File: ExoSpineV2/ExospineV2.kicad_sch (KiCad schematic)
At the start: 49 parts, among them J1 GPIO, J15 Conn_01x02, J16 Conn_01x02, J17 Conn_01x02, J19 Conn_01x03, J20 Conn_01x03, J21 Conn_01x03, J22 Conn_01x02, J23 Conn_01x02, J24 Conn_01x02, J25 Conn_01x03, J26 JST PH 3pin, J27 Conn_01x04, J29 Conn_01x03, J30 Conn_01x02, J34 Conn_01x03, Q10 Q_NMOS_DGS, Q11 Q_NMOS_DGS, Q6 Q_NMOS_DGS, Q7 Q_NMOS_DGS, Q8 Q_NMOS_DGS, Q9 Q_NMOS_DGS, U4 74HC00, U5 74HC00, U6 MCP3008, U7 LTC2944, U8 LTC2944

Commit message: added connectors
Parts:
- J15, J16, J17, J22, J23, J24, J30: value Conn_01x02 -> JST PH 2pin; footprint (none) -> Connector_JST:JST_PH_B2B-PH-K_1x02_P2.00mm_Vertical
- J19, J20, J21, J25, J29, J34: value Conn_01x03 -> JST PH 3pin; footprint (none) -> Connector_JST:JST_PH_B3B-PH-K_1x03_P2.00mm_Vertical
- J26: footprint Connector_JST:JST_PH_B2B-PH-K_1x02_P2.00mm_Vertical -> Connector_JST:JST_PH_B3B-PH-K_1x03_P2.00mm_Vertical
- J27: value Conn_01x04 -> JST PH 4pin; footprint (none) -> Connector_JST:JST_PH_B4B-PH-K_1x04_P2.00mm_Vertical
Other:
- note added: "Batterie Feedback Switch - 0 for 12V Battery - 1 for 24V Battery"
- note removed: "12V Batterie I2C Enable"
- note removed: "24V Batterie I2C Enable"
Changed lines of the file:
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@@
     (fill (type none))
   )
-  (arc (start 46.936 71.123) (mid 46.1743 68.5836) (end 46.932 66.043)
+  (arc (start 46.99 68.58) (mid 46.4298 67.3236) (end 46.932 66.043)
     (stroke (width 0) (type default) (color 132 132 132 1))
     (fill (type none))
@@
     (effects (font (size 1.27 1.27)) (justify left bottom))
   )
-  (text "12V Batterie I2C Enable" (at 45.72 68.58 0)
-    (effects (font (size 1.27 1.27) (color 132 132 132 1)) (justify right bottom))
-  )
   (text "Button" (at 119.38 66.04 0)
     (effects (font (size 1.27 1.27) (color 132 132 132 1)) (justify left bottom))
@@
     (effects (font (size 1.27 1.27)) (justify left bottom))
   )
-  (text "24V Batterie I2C Enable" (at 45.72 71.12 0)
-    (effects (font (size 1.27 1.27) (color 132 132 132 1)) (justify right bottom))
-  )
   (text "Actuator Feedback 2" (at 299.72 177.8 0)
     (effects (font (size 1.27 1.27)) (justify left bottom))
@@
     (effects (font (size 1.27 1.27) (color 132 132 132 1)) (justify left bottom))
   )
+  (text "Batterie Feedback Switch\n- 0 for 12V Battery\n- 1 for 24V Battery"
+    (at 21.59 72.39 0)
+    (effects (font (size 1.27 1.27) (color 132 132 132 1)) (justify left bottom))
+  )
   (text "SN74HC00DR" (at 316.23 185.42 0)
     (effects (font (size 1.27 1.27) (color 0 194 0 1)) (justify left bottom))
@@
       (effects (font (size 1.27 1.27)) (justify left))
     )
-    (property "Value" "Conn_01x02" (at 346.71 33.02 0)
+    (property "Value" "JST PH 2pin" (at 346.71 33.02 0)
       (effects (font (size 1.27 1.27)) (justify left))
     )
-    (property "Footprint" "" (at 344.17 30.48 0)
+    (property "Footprint" "Connector_JST:JST_PH_B2B-PH-K_1x02_P2.00mm_Vertical" (at 344.17 30.48 0)
       (effects (font (size 1.27 1.27)) hide)
     )
@@
       (effects (font (size 1.27 1.27)) (justify left))
     )
-    (property "Value" "Conn_01x03" (at 284.48 191.77 0)
+    (property "Value" "JST PH 3pin" (at 284.48 191.77 0)
       (effects (font (size 1.27 1.27)) (justify left))
     )
-    (property "Footprint" "" (at 281.94 190.5 0)
+    (property "Footprint" "Connector_JST:JST_PH_B3B-PH-K_1x03_P2.00mm_Vertical" (at 281.94 190.5 0)
       (effects (font (size 1.27 1.27)) hide)
     )
@@
       (effects (font (size 1.27 1.27)) (justify left))
     )
-    (property "Value" "Conn_01x02" (at 250.19 69.85 0)
+    (property "Value" "JST PH 2pin" (at 250.19 69.85 0)
       (effects (font (size 1.27 1.27)) (justify left))
     )
-    (property "Footprint" "" (at 247.65 67.31 0)
+    (property "Footprint" "Connector_JST:JST_PH_B2B-PH-K_1x02_P2.00mm_Vertical" (at 247.65 67.31 0)
       (effects (font (size 1.27 1.27)) hide)
     )
@@
       (effects (font (size 1.27 1.27)) (justify left))
     )
-    (property "Value" "Conn_01x03" (at 304.8 156.21 0)
+    (property "Value" "JST PH 3pin" (at 304.8 156.21 0)
       (effects (font (size 1.27 1.27)) (justify left))
     )
-    (property "Footprint" "" (at 302.26 154.94 0)
+    (property "Footprint" "Connector_JST:JST_PH_B3B-PH-K_1x03_P2.00mm_Vertical" (at 302.26 154.94 0)
       (effects (font (size 1.27 1.27)) hide)
     )
@@
       (effects (font (size 1.27 1.27)) (justify left))
     )
-    (property "Value" "Conn_01x03" (at 374.65 191.77 0)
+    (property "Value" "JST PH 3pin" (at 374.65 191.77 0)
       (effects (font (size 1.27 1.27)) (justify left))
     )
-    (property "Footprint" "" (at 372.11 190.5 0)
+    (property "Footprint" "Connector_JST:JST_PH_B3B-PH-K_1x03_P2.00mm_Vertical" (at 372.11 190.5 0)
       (effects (font (size 1.27 1.27)) hide)
     )
@@
       (effects (font (size 1.27 1.27)) (justify left))
     )
-    (property "Footprint" "Connector_JST:JST_PH_B2B-PH-K_1x02_P2.00mm_Vertical" (at 284.48 33.02 0)
+    (property "Footprint" "Connector_JST:JST_PH_B3B-PH-K_1x03_P2.00mm_Vertical" (at 284.48 33.02 0)
       (effects (font (size 1.27 1.27)) hide)
     )
@@
       (effects (font (size 1.27 1.27)) (justify left))
     )
-    (property "Value" "Conn_01x03" (at 361.95 156.21 0)
+    (property "Value" "JST PH 3pin" (at 361.95 156.21 0)
       (effects (font (size 1.27 1.27)) (justify left))
     )
-    (property "Footprint" "" (at 359.41 154.94 0)
+    (property "Footprint" "Connector_JST:JST_PH_B3B-PH-K_1x03_P2.00mm_Vertical" (at 359.41 154.94 0)
       (effects (font (size 1.27 1.27)) hide)
     )
@@
       (effects (font (size 1.27 1.27)) (justify left))
     )
-    (property "Value" "Conn_01x03" (at 408.94 36.83 0)
+    (property "Value" "JST PH 3pin" (at 408.94 36.83 0)
       (effects (font (size 1.27 1.27)) (justify left))
     )
-    (property "Footprint" "" (at 406.4 35.56 0)
+    (property "Footprint" "Connector_JST:JST_PH_B3B-PH-K_1x03_P2.00mm_Vertical" (at 406.4 35.56 0)
       (effects (font (size 1.27 1.27)) hide)
     )
@@
       (effects (font (size 1.27 1.27)) (justify left))
     )
-    (property "Value" "Conn_01x02" (at 364.49 111.76 0)
+    (property "Value" "JST PH 2pin" (at 364.49 111.76 0)
       (effects (font (size 1.27 1.27)) (justify left))
     )
-    (property "Footprint" "" (at 361.95 109.22 0)
+    (property "Footprint" "Connector_JST:JST_PH_B2B-PH-K_1x02_P2.00mm_Vertical" (at 361.95 109.22 0)
       (effects (font (size 1.27 1.27)) hide)
     )
@@
       (effects (font (size 1.27 1.27)) (justify left))
     )
-    (property "Value" "Conn_01x02" (at 250.19 111.76 0)
+    (property "Value" "JST PH 2pin" (at 250.19 111.76 0)
       (effects (font (size 1.27 1.27)) (justify left))
     )
-    (property "Footprint" "" (at 247.65 109.22 0)
+    (property "Footprint" "Connector_JST:JST_PH_B2B-PH-K_1x02_P2.00mm_Vertical" (at 247.65 109.22 0)
       (effects (font (size 1.27 1.27)) hide)
     )
@@
       (effects (font (size 1.27 1.27)) (justify left))
     )
-    (property "Value" "Conn_01x02" (at 364.49 69.85 0)
+    (property "Value" "JST PH 2pin" (at 364.49 69.85 0)
       (effects (font (size 1.27 1.27)) (justify left))
     )
-    (property "Footprint" "" (at 361.95 67.31 0)
+    (property "Footprint" "Connector_JST:JST_PH_B2B-PH-K_1x02_P2.00mm_Vertical" (at 361.95 67.31 0)
       (effects (font (size 1.27 1.27)) hide)
     )
@@
       (effects (font (size 1.27 1.27)) (justify left))
     )
-    (property "Value" "Conn_01x03" (at 247.65 156.21 0)
+    (property "Value" "JST PH 3pin" (at 247.65 156.21 0)
       (effects (font (size 1.27 1.27)) (justify left))
     )
-    (property "Footprint" "" (at 245.11 154.94 0)
+    (property "Footprint" "Connector_JST:JST_PH_B3B-PH-K_1x03_P2.00mm_Vertical" (at 245.11 154.94 0)
       (effects (font (size 1.27 1.27)) hide)
     )
@@
       (effects (font (size 1.27 1.27)) (justify left))
     )
-    (property "Value" "Conn_01x02" (at 307.34 69.85 0)
+    (property "Value" "JST PH 2pin" (at 307.34 69.85 0)
       (effects (font (size 1.27 1.27)) (justify left))
     )
-    (property "Footprint" "" (at 304.8 67.31 0)
+    (property "Footprint" "Connector_JST:JST_PH_B2B-PH-K_1x02_P2.00mm_Vertical" (at 304.8 67.31 0)
       (effects (font (size 1.27 1.27)) hide)
     )
@@
       (effects (font (size 1.27 1.27)) (justify left))
     )
-    (property "Value" "Conn_01x02" (at 307.34 111.76 0)
+    (property "Value" "JST PH 2pin" (at 307.34 111.76 0)
       (effects (font (size 1.27 1.27)) (justify left))
     )
-    (property "Footprint" "" (at 304.8 109.22 0)
+    (property "Footprint" "Connector_JST:JST_PH_B2B-PH-K_1x02_P2.00mm_Vertical" (at 304.8 109.22 0)
       (effects (font (size 1.27 1.27)) hide)
     )
@@
       (effects (font (size 1.27 1.27)) (justify left))
     )
-    (property "Value" "Conn_01x04" (at 236.22 34.29 0)
+    (property "Value" "JST PH 4pin" (at 236.22 34.29 0)
       (effects (font (size 1.27 1.27)) (justify left))
     )
-    (property "Footprint" "" (at 233.68 31.75 0)
+    (property "Footprint" "Connector_JST:JST_PH_B4B-PH-K_1x04_P2.00mm_Vertical" (at 233.68 31.75 0)
       (effects (font (size 1.27 1.27)) hide)
     )

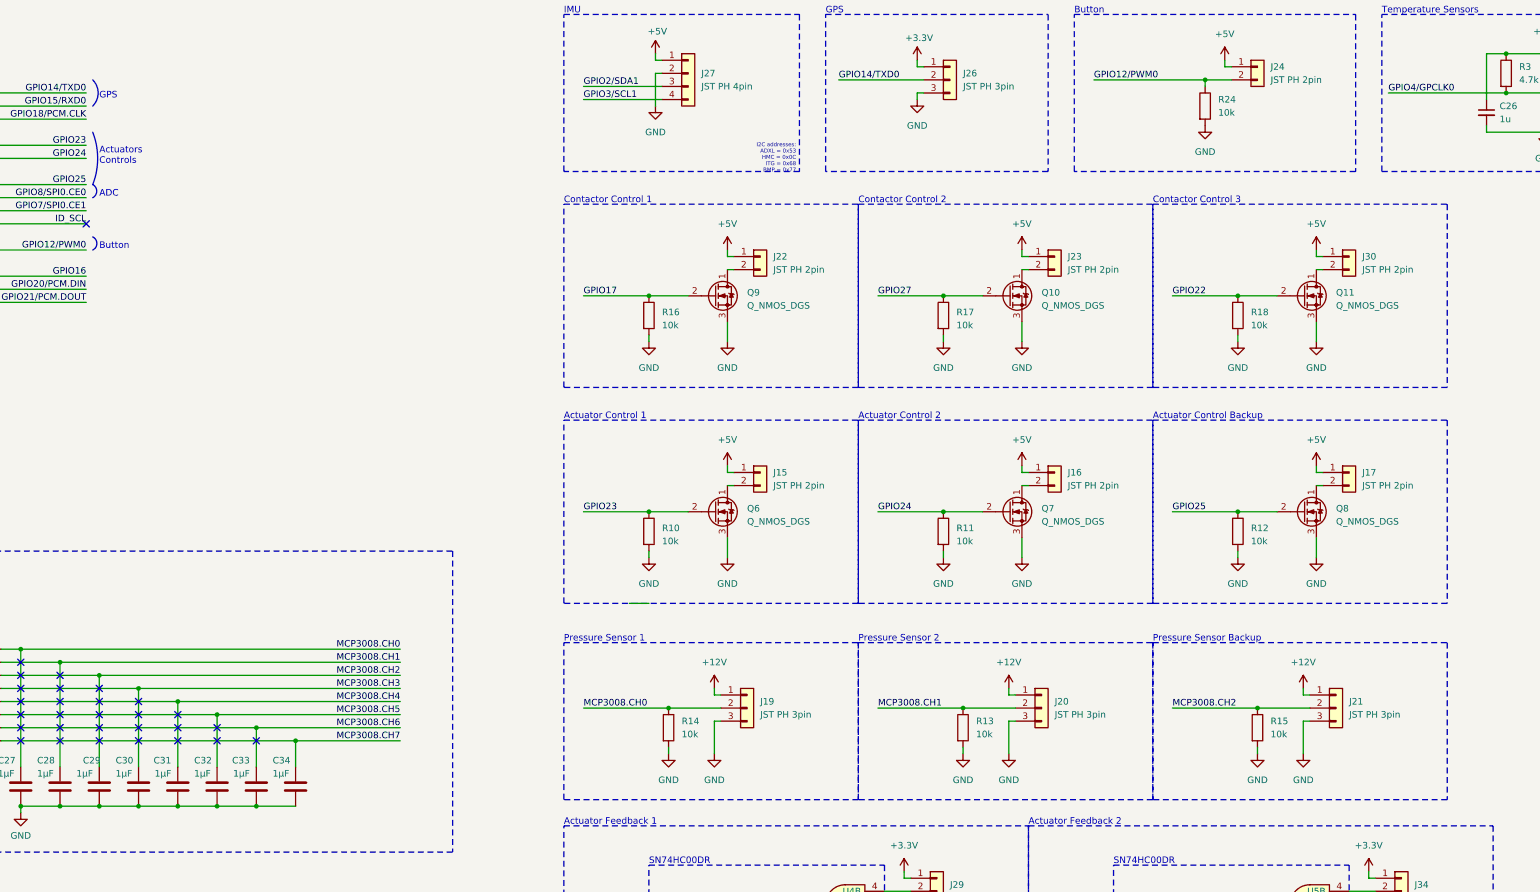
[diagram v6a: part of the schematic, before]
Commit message: chose 10k resistors on JLCPCB (datasheets & footprints)
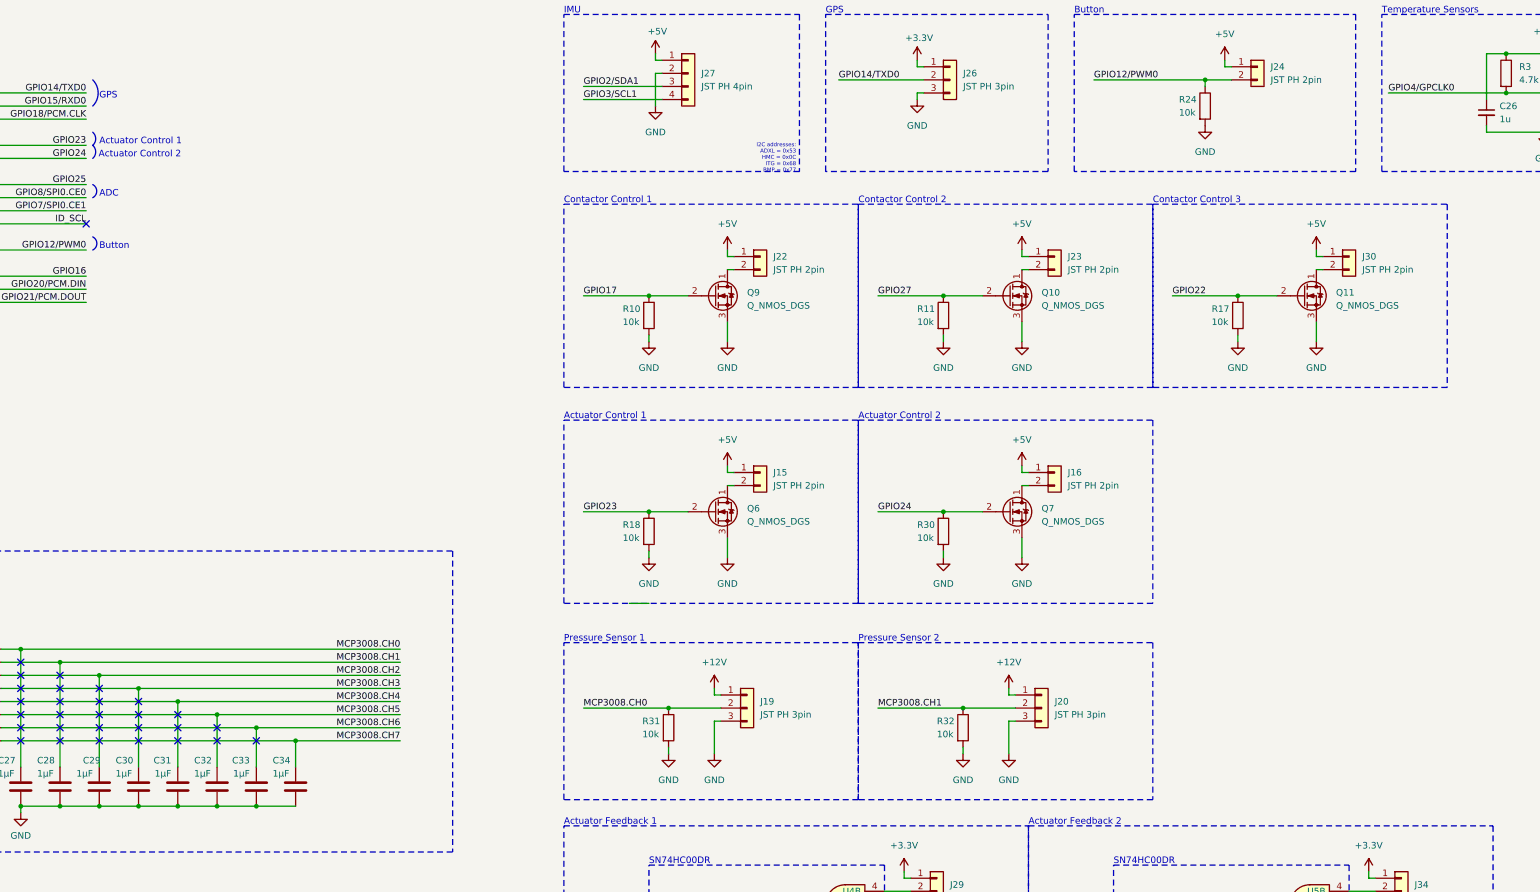
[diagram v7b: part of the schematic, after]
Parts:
- removed J17: JST PH 2pin, Connector_JST:JST_PH_B2B-PH-K_1x02_P2.00mm_Vertical, symbol Connector_Generic:Conn_01x02
- removed J21: JST PH 3pin, Connector_JST:JST_PH_B3B-PH-K_1x03_P2.00mm_Vertical, symbol Connector_Generic:Conn_01x03
- removed Q8: Q_NMOS_DGS, symbol Device:Q_NMOS_DGS
- removed R12, R13, R14, R15, R16: 10k, symbol Device:R
- added R30, R31, R32: 10k, Resistor_SMD:R_0402_1005Metric, symbol Device:R
- R10, R11, R17, R18, R24: footprint (none) -> Resistor_SMD:R_0402_1005Metric; JLCPCB (none) -> https://jlcpcb.com/partdetail/26487-0402WGF1002TCE/C25744
- R3: JLCPCB (none) -> https://jlcpcb.com/partdetail/26643-0402WGF4701TCE/C25900
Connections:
- net GND: now also R30.2, R31.2, R32.2
- net GPIO17: now also R10.1
- net GPIO22: now also R17.1; no longer R18.1
- net GPIO23: now also R18.1; no longer R10.1
- net GPIO24: now also R30.1; no longer R11.1
- net GPIO27: now also R11.1; no longer R17.1
- net MCP3008.CH0: now also R31.1
- net MCP3008.CH1: now also R32.1
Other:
- note removed: "Actuator Control Backup"
- note removed: "Actuators Controls"
- note removed: "Pressure Sensor Backup"
